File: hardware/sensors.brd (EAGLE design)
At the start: 80 x 80 mm, 28 parts, among them J1 CDH, J2 OW, J3 DBG, J4 SUN-UART, J5 ADCS, J6 ENV, J7 SUN, U1 DS18B20, U2 DS18B20, U3 DS18B20

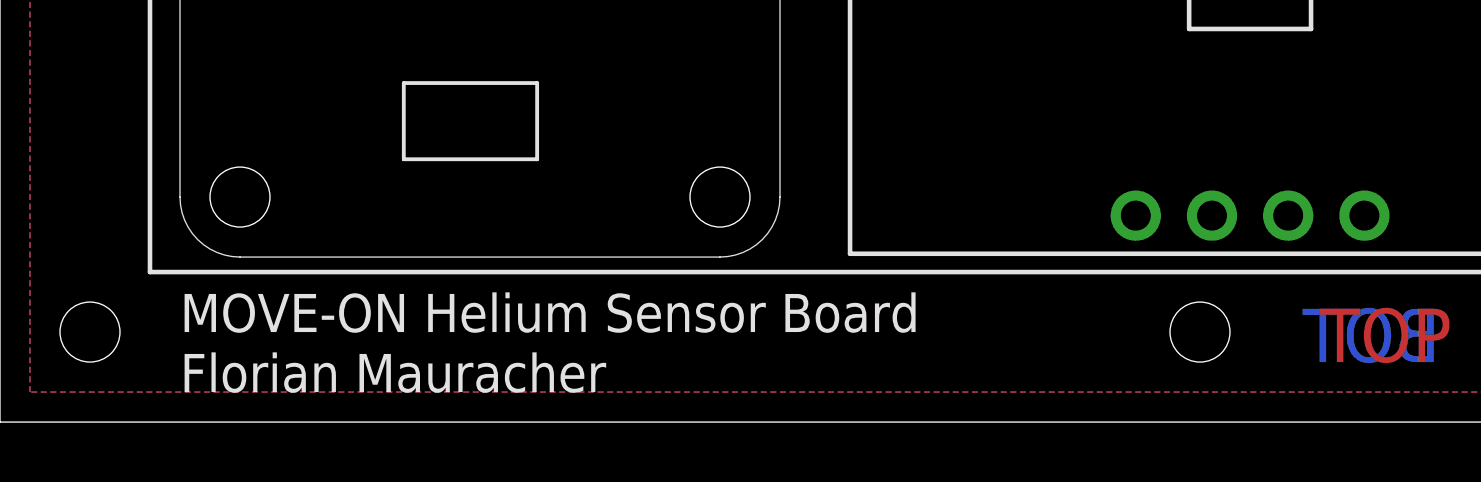
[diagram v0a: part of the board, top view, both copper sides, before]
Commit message: Update pin names to match sw
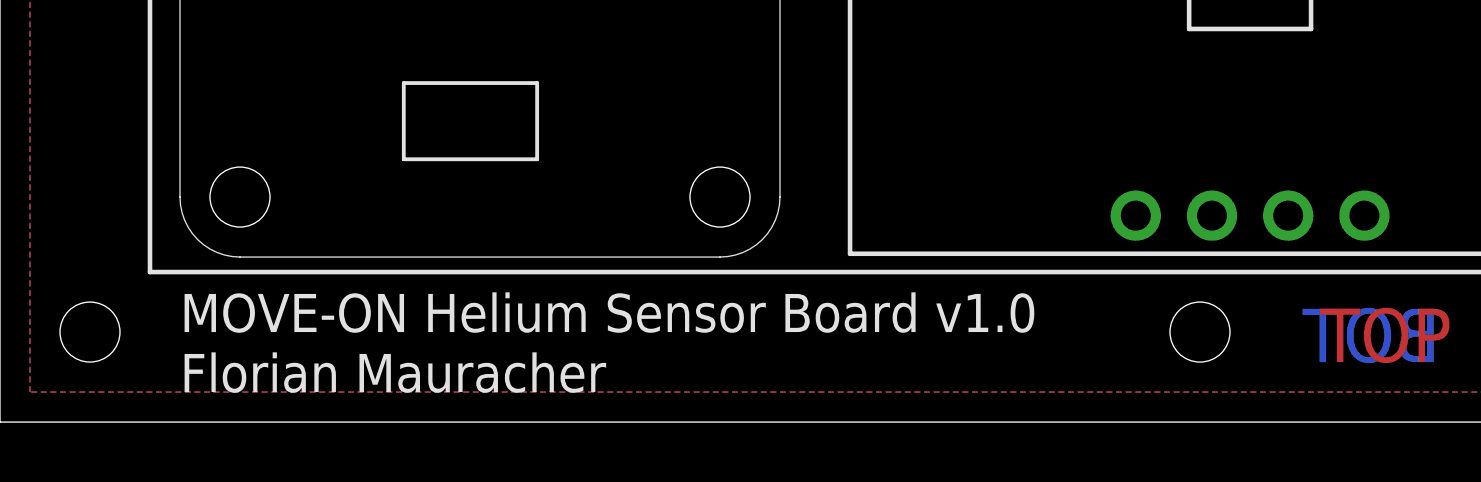
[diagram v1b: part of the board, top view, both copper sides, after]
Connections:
- net LOG-UART renamed LOG-TX
- net SPI-CS-ENO renamed SPI-CS-ENV1
- net SPI-CS-ENV renamed SPI-CS-ENV0
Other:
- board text added: "MOVE-ON Helium Sensor Board v1.0"
- board text removed: "MOVE-ON Helium Sensor Board"
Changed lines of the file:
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@@
 <hole x="40" y="3" drill="2"/>
 <text x="4" y="6" size="1.27" layer="25" rot="R90">&gt;LAST_DATE_TIME</text>
-<text x="6" y="3" size="1.27" layer="25">MOVE-ON Helium Sensor Board</text>
+<text x="6" y="3" size="1.27" layer="25">MOVE-ON Helium Sensor Board v1.0</text>
 <text x="6" y="1" size="1.27" layer="25">Florian Mauracher</text>
 <rectangle x1="57" y1="67" x2="80" y2="80" layer="41"/>
@@
 <wire x1="64.460425" y1="48.258" x2="62.932" y2="48.258" width="0.3048" layer="16"/>
 </signal>
-<signal name="LOG-UART">
+<signal name="LOG-TX">
 <contactref element="B4" pad="RXI"/>
 <contactref element="B1" pad="A7"/>
@@
 <via x="44" y="42" extent="1-16" drill="0.508"/>
 </signal>
-<signal name="SPI-CS-ENV">
+<signal name="SPI-CS-ENV0">
 <contactref element="B1" pad="D3"/>
 <contactref element="J6" pad="1"/>
@@
 <wire x1="34.708" y1="31.292" x2="30.89" y2="35.11" width="0.3048" layer="16"/>
 </signal>
-<signal name="SPI-CS-ENO">
+<signal name="SPI-CS-ENV1">
 <contactref element="B1" pad="D13"/>
 <contactref element="B5" pad="CS"/>

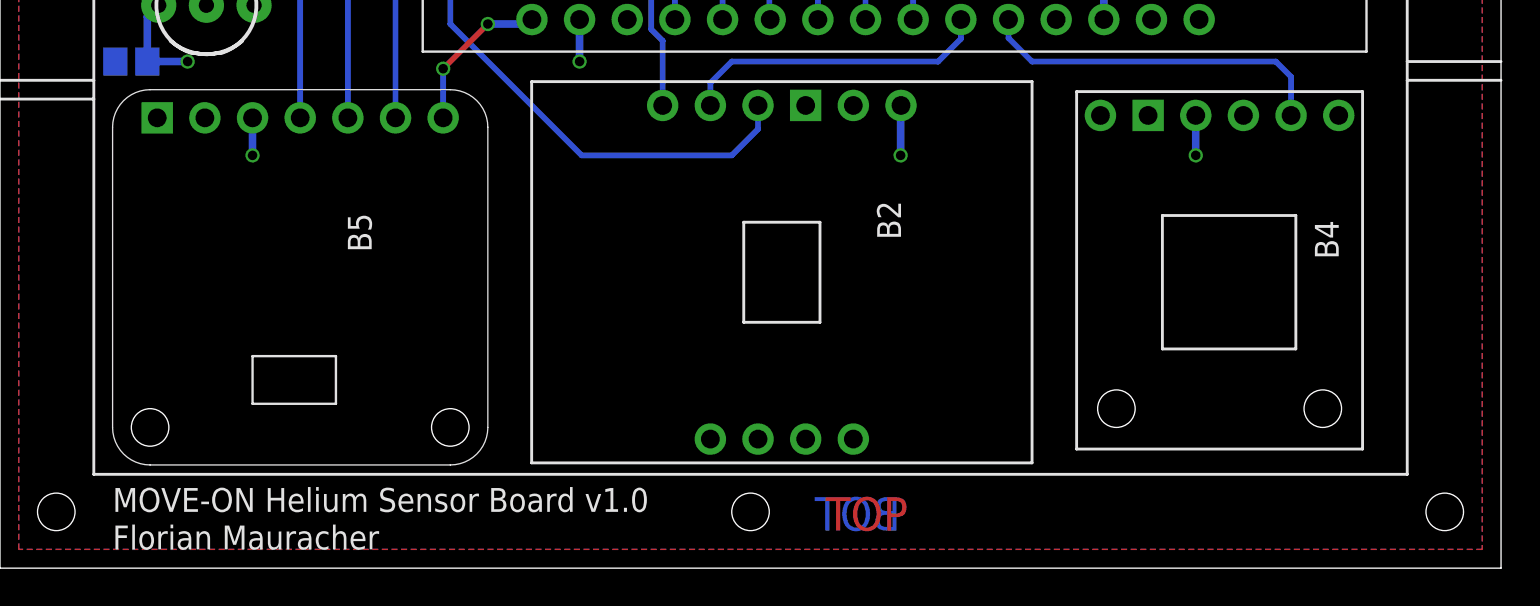
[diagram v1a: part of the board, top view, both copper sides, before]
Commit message: Add HM-11 module as alternative to OpenLog
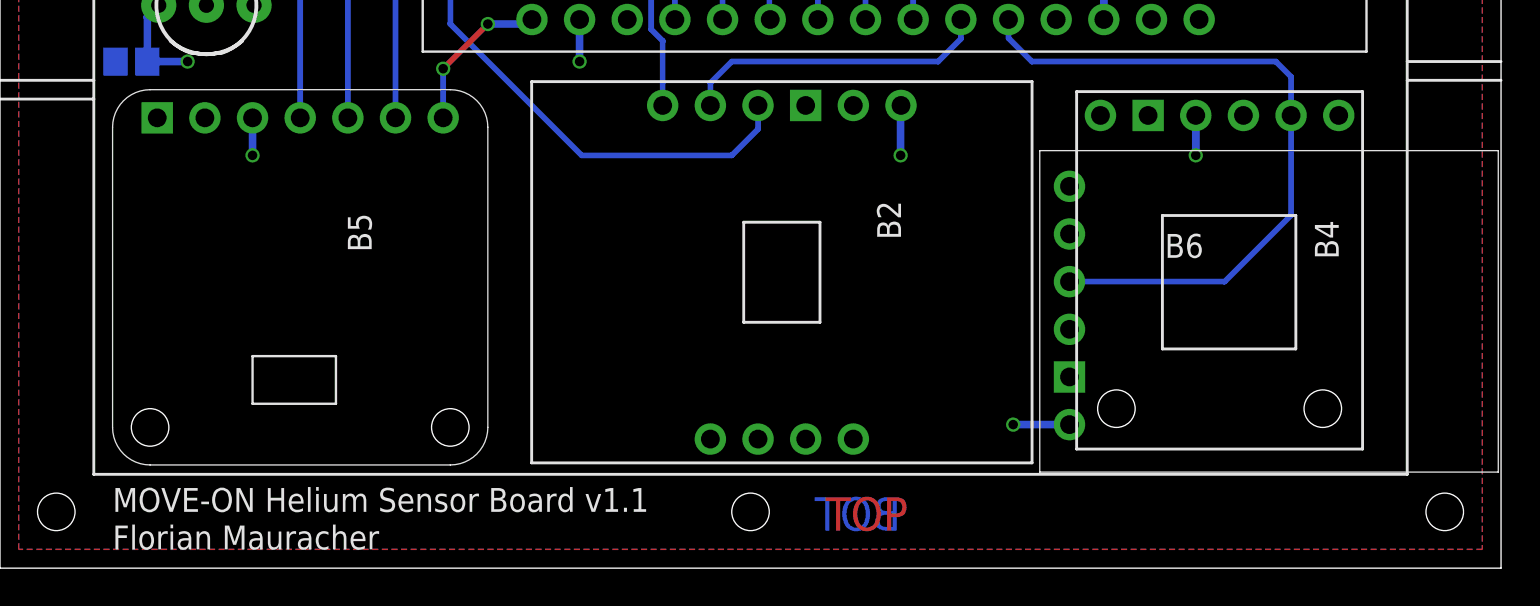
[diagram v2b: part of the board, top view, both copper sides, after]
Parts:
- added B6: (no value), Frcy:HUAMAO-HM-11
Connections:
- net GND: now also B6.GND
- net LOG-TX: now also B6.RX
- net VCC: now also B6.VCC
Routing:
- net LOG-TX: track 19.0 -> 37.6 mm
- net VCC: track 84.0 -> 87.0 mm, vias 17 -> 18
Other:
- board text added: "MOVE-ON Helium Sensor Board v1.1"
- board text removed: "MOVE-ON Helium Sensor Board v1.0"
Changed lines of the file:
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@@
 <hole x="40" y="3" drill="2"/>
 <text x="4" y="6" size="1.27" layer="25" rot="R90">&gt;LAST_DATE_TIME</text>
-<text x="6" y="3" size="1.27" layer="25">MOVE-ON Helium Sensor Board v1.0</text>
+<text x="6" y="3" size="1.27" layer="25">MOVE-ON Helium Sensor Board v1.1</text>
 <text x="6" y="1" size="1.27" layer="25">Florian Mauracher</text>
 <rectangle x1="57" y1="67" x2="80" y2="80" layer="41"/>
@@
 <attribute name="SPICEPREFIX" value="C" x="27" y="74" size="1.778" layer="28" rot="MR180" display="off"/>
 </element>
+<element name="B6" library="Frcy" package="HUAMAO-HM-11" value="" x="57" y="14" rot="R270"/>
 </elements>
 <signals>
@@
 <wire x1="8.46" y1="30" x2="7.85" y2="29.39" width="0.4064" layer="16"/>
 <wire x1="7.85" y1="29.39" x2="7.85" y2="27" width="0.4064" layer="16"/>
+<contactref element="B6" pad="VCC"/>
+<wire x1="57" y1="7.65" x2="54" y2="7.65" width="0.4064" layer="16"/>
+<via x="54" y="7.65" extent="1-16" drill="0.508"/>
 </signal>
 <signal name="GND">
@@
 <contactref element="C9" pad="1"/>
 <contactref element="C10" pad="1"/>
+<contactref element="B6" pad="GND"/>
 </signal>
 <signal name="IMU-SDA">
@@
 <wire x1="68" y1="27" x2="68.81" y2="26.19" width="0.3048" layer="16"/>
 <wire x1="68.81" y1="26.19" x2="68.81" y2="24.128" width="0.3048" layer="16"/>
+<contactref element="B6" pad="RX"/>
+<wire x1="68.81" y1="24.128" x2="68.81" y2="18.81" width="0.3048" layer="16"/>
+<wire x1="65.27" y1="15.27" x2="57" y2="15.27" width="0.3048" layer="16"/>
+<wire x1="68.81" y1="18.81" x2="65.27" y2="15.27" width="0.3048" layer="16"/>
 </signal>
 <signal name="CDH-TX">

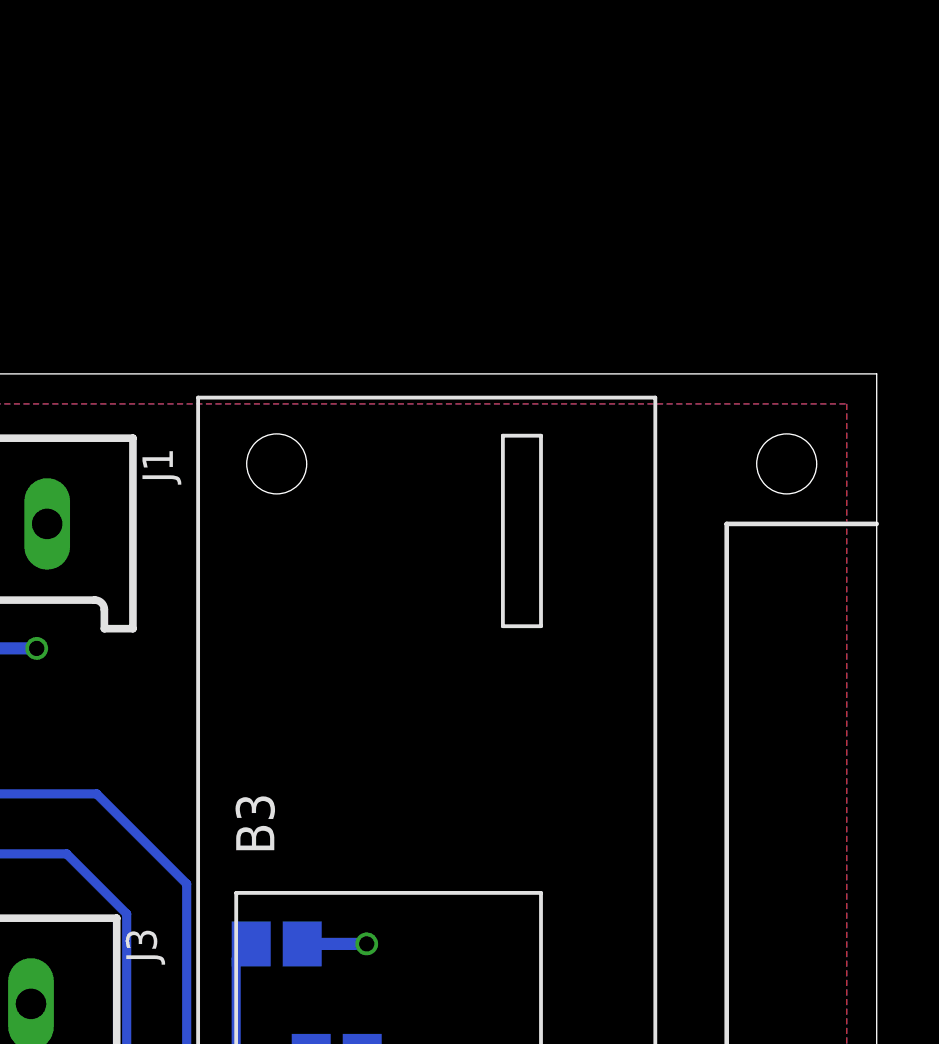
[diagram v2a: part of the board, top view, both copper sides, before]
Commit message: Add GPS chip with external antenna
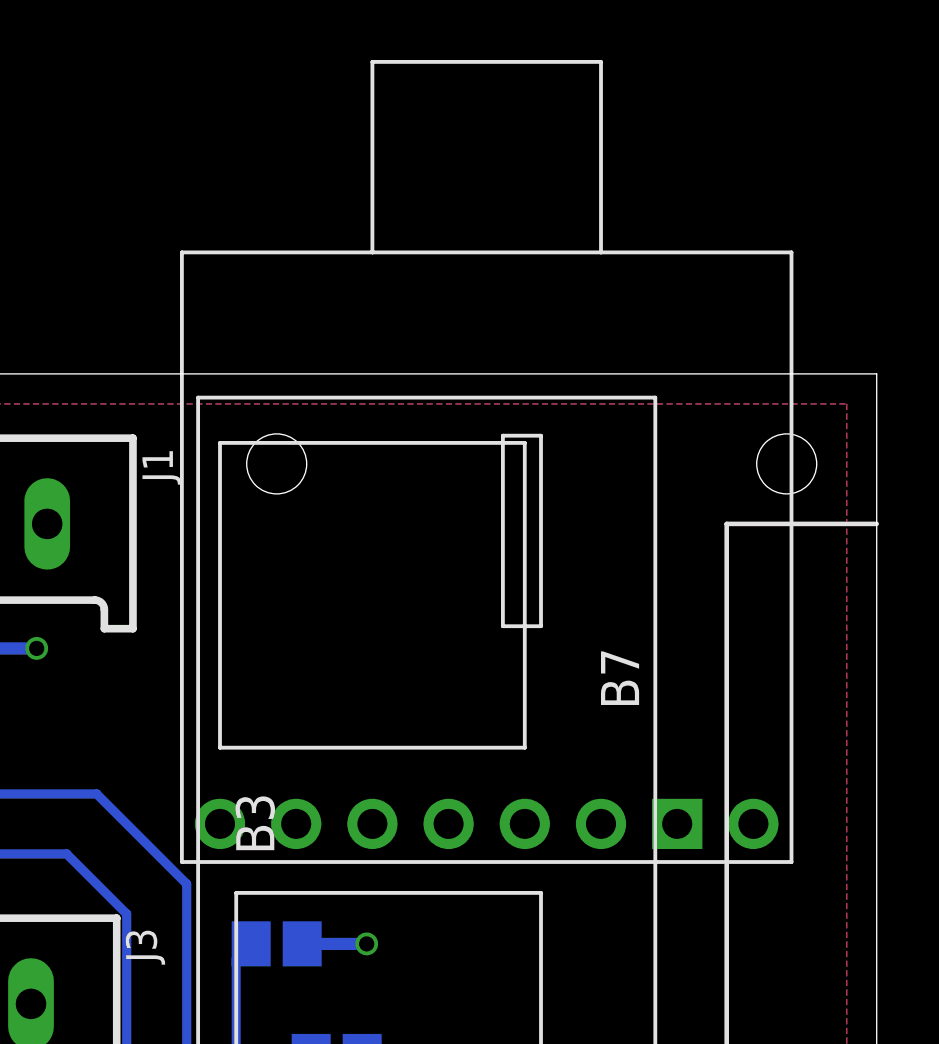
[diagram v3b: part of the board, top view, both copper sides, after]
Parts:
- added B7: UBLOX2, Frcy:UPUTRONICS-UBLOX-M8Q
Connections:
- new net GPS-TP: B7.TP1, B7.TP2
- net GND: now also B7.GND
- net GPS-RX: now also B7.RXD
- net GPS-SCL: now also B7.SCL
- net GPS-SDA: now also B7.SDA
- net GPS-TX: now also B7.TXD
- net VCC: now also B7.VCC
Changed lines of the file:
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@@
 <?xml version="1.0" encoding="utf-8"?>
 <!DOCTYPE eagle SYSTEM "eagle.dtd">
-<eagle version="8.6.0">
+<eagle version="9.0.0">
 <drawing>
 <settings>
@@
 </element>
 <element name="B6" library="Frcy" package="HUAMAO-HM-11" value="" x="57" y="14" rot="R270"/>
+<element name="B7" library="Frcy" package="UPUTRONICS-UBLOX-M8Q" value="UBLOX2" x="67" y="65"/>
 </elements>
 <signals>
@@
 <wire x1="57" y1="7.65" x2="54" y2="7.65" width="0.4064" layer="16"/>
 <via x="54" y="7.65" extent="1-16" drill="0.508"/>
+<contactref element="B7" pad="VCC"/>
+<wire x1="54" y1="7.65" x2="75.89" y2="65" width="0" layer="19" extent="16-16"/>
 </signal>
 <signal name="GND">
@@
 <contactref element="C10" pad="1"/>
 <contactref element="B6" pad="GND"/>
+<contactref element="B7" pad="GND"/>
+<wire x1="57" y1="10.19" x2="73.35" y2="65" width="0" layer="19" extent="1-1"/>
 </signal>
 <signal name="IMU-SDA">
@@
 <wire x1="48.67" y1="43.33" x2="50" y2="42" width="0.3048" layer="16"/>
 <wire x1="50" y1="42" x2="64" y2="42" width="0.3048" layer="16"/>
+<contactref element="B7" pad="SDA"/>
+<wire x1="59.15" y1="61" x2="58.11" y2="65" width="0" layer="19" extent="16-16"/>
 </signal>
 <signal name="GPS-SCL">
@@
 <wire x1="62.932" y1="48.258" x2="61.19" y2="50" width="0.3048" layer="16"/>
 <wire x1="64.460425" y1="48.258" x2="62.932" y2="48.258" width="0.3048" layer="16"/>
+<contactref element="B7" pad="SCL"/>
+<wire x1="61.15" y1="57.25" x2="60.65" y2="65" width="0" layer="19" extent="16-16"/>
 </signal>
 <signal name="LOG-TX">
@@
 <wire x1="53" y1="52" x2="49.27" y2="55.73" width="0.3048" layer="16"/>
 <wire x1="49.27" y1="55.73" x2="49.27" y2="59" width="0.3048" layer="16"/>
+<contactref element="B7" pad="TXD"/>
+<wire x1="63" y1="52" x2="63.19" y2="65" width="0" layer="19" extent="16-16"/>
 </signal>
 <signal name="GPS-RX">
@@
 <wire x1="53" y1="54" x2="51.81" y2="55.19" width="0.3048" layer="16"/>
 <wire x1="51.81" y1="55.19" x2="51.81" y2="59" width="0.3048" layer="16"/>
+<contactref element="B7" pad="RXD"/>
+<wire x1="65.27" y1="54" x2="65.73" y2="65" width="0" layer="19" extent="16-16"/>
 </signal>
 <signal name="SPI-CS-SUN">
@@
 <wire x1="23.62" y1="26.62" x2="23.62" y2="24" width="0.3048" layer="16"/>
 </signal>
+<signal name="GPS-TP">
+<contactref element="B7" pad="TP1"/>
+<contactref element="B7" pad="TP2"/>
+<wire x1="70.81" y1="65" x2="68.27" y2="65" width="0" layer="19" extent="1-1"/>
+</signal>
 </signals>

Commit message: Connect external GPS chip on board
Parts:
- moved R6 22.0 mm to (60.0, 39.0)
- moved R5 21.3 mm to (60.0, 36.0)
- moved B7 4.03 mm to (67.5, 61.0)
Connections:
- removed net DBG-RX: B1.A4, J3.3
- net GPS-TP: now also B1.A4, J3.3
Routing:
- net GPS-TP: track 0.00 -> 75.7 mm, vias 0 -> 2
- net DBG-RX: track 33.2 -> 0.00 mm
- net GPS-SCL: track 40.1 -> 51.8 mm
- net GPS-TX: track 20.8 -> 30.4 mm
- net GPS-RX: track 22.2 -> 29.8 mm
- net GPS-SDA: track 42.5 -> 46.8 mm, vias 0 -> 2
- net VCC: track 87.0 -> 89.2 mm, vias 18 -> 19

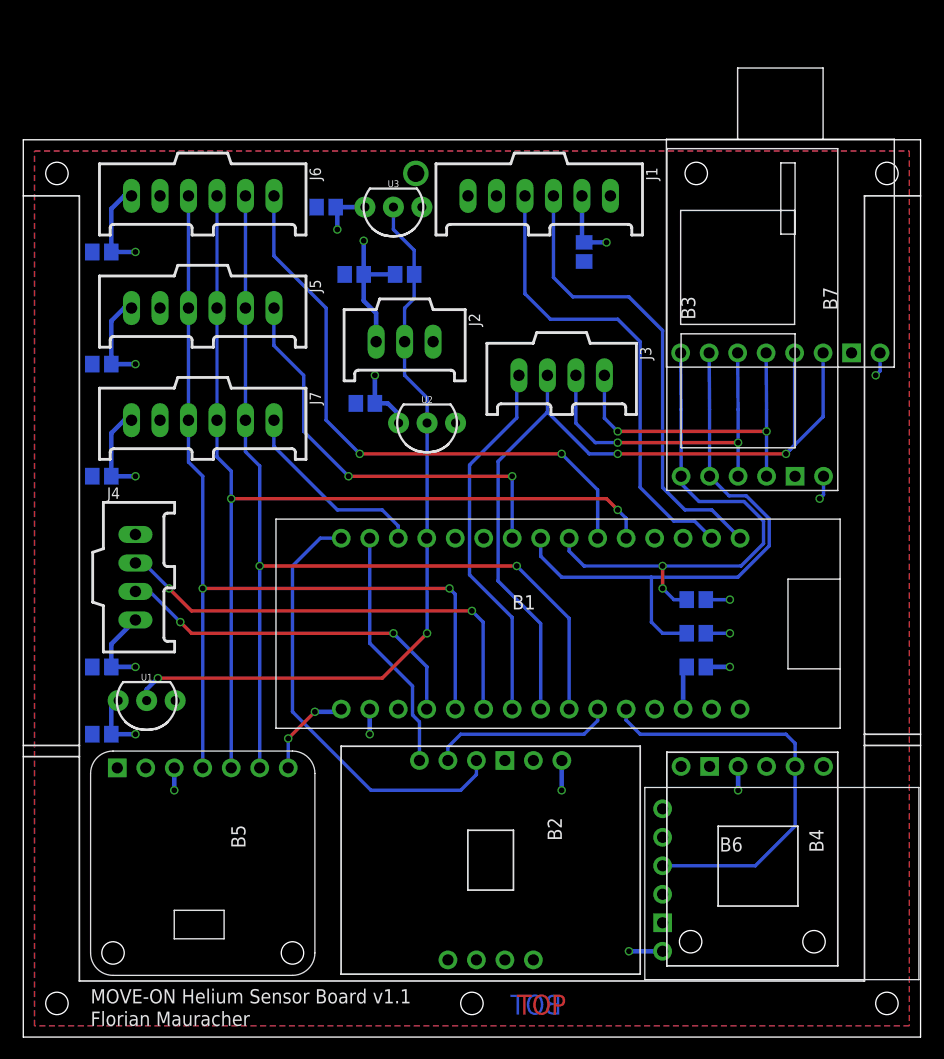
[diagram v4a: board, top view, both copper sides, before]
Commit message: Update component names
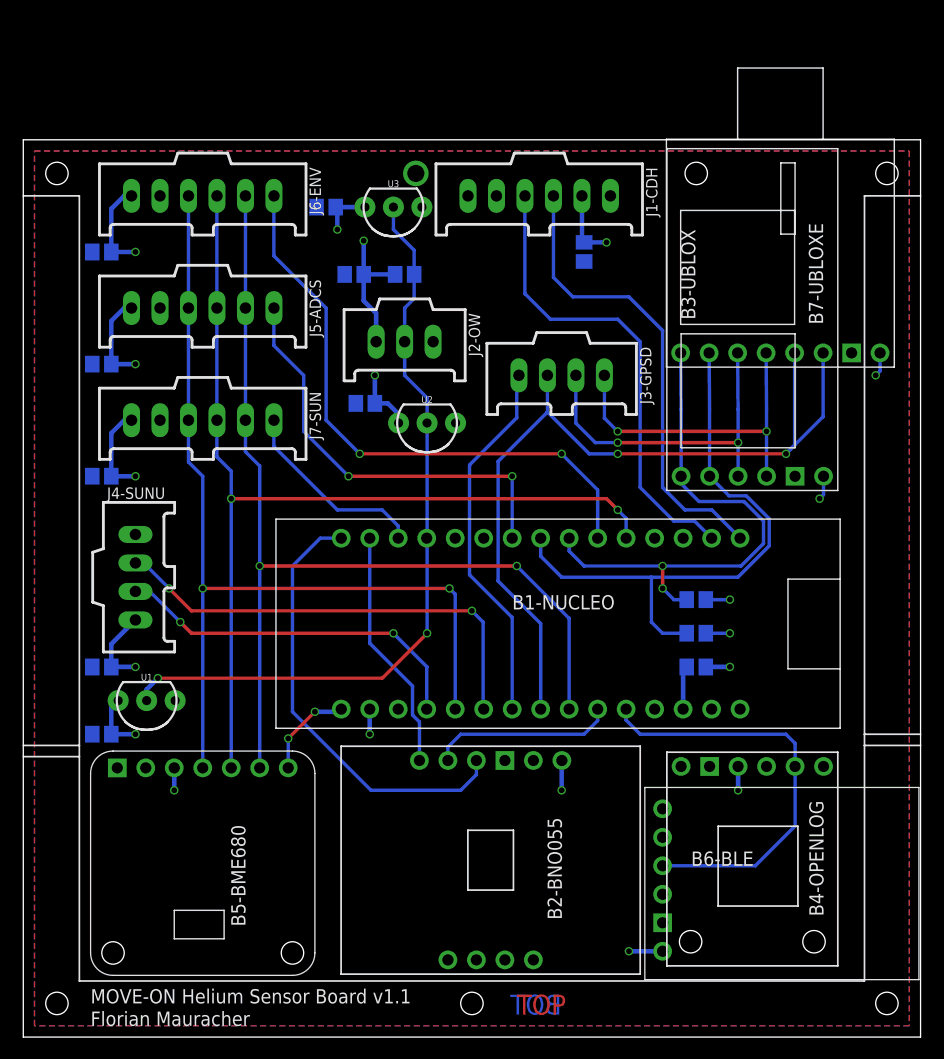
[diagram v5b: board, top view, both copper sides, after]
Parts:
- B1-NUCLEO: value NUCLEO-32 -> (none)
- B2-BNO055: value BNO055 -> (none)
- B3-UBLOX: value UBLOX -> (none)
- B4-OPENLOG: value OPENLOG -> (none)
- B5-BME680: value BME680 -> (none)
- B7-UBLOXE: value UBLOX2 -> (none)
- J1-CDH: value CDH -> (none)
- J2-OW: value OW -> (none)
- J3-GPSD: value DBG -> (none)
- J4-SUNU: value SUN-UART -> (none)
- J5-ADCS: value ADCS -> (none)
- J6-ENV: value ENV -> (none)
- J7-SUN: value SUN -> (none)
- renumbered B1 to B1-NUCLEO, B2 to B2-BNO055, B3 to B3-UBLOX, B4 to B4-OPENLOG, B5 to B5-BME680, B6 to B6-BLE, B7 to B7-UBLOXE, J1 to J1-CDH, J2 to J2-OW, J3 to J3-GPSD, J4 to J4-SUNU, J5 to J5-ADCS, J6 to J6-ENV, J7 to J7-SUN
